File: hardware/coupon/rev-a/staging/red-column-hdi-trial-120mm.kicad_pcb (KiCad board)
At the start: 6 copper layers, 120 x 32.5 mm, 497 parts, among them J1 USB4505-03-0-A, J2 S2B-PH-SM4-TB, Q1 DMP2066LSN-7, Q10 DMP2066LSN-7, Q11 DMP2066LSN-7, Q12 DMP2066LSN-7, Q13 DMP2066LSN-7, Q14 DMP2066LSN-7, Q15 DMP2066LSN-7, Q16 DMP2066LSN-7, Q17 2N7002K-7, Q18 2N7002K-7, Q19 2N7002K-7, Q2 DMP2066LSN-7, Q20 2N7002K-7, Q21 2N7002K-7, Q22 2N7002K-7, Q23 2N7002K-7, Q24 2N7002K-7, Q25 2N7002K-7, Q26 2N7002K-7, Q27 2N7002K-7, Q28 2N7002K-7, Q29 2N7002K-7, Q3 DMP2066LSN-7, Q30 2N7002K-7, Q31 2N7002K-7, Q32 2N7002K-7, Q4 DMP2066LSN-7, Q5 DMP2066LSN-7, Q6 DMP2066LSN-7, Q7 DMP2066LSN-7, Q8 DMP2066LSN-7, Q9 DMP2066LSN-7, SW1 EVQP7J01P, SW2 JS202011JCQN, U1 TLC59581RTQT, U11 SN74LVC1G04DBVR, U17 SN74LVC1G11DBVR, U2 74HC4514PW,118, U23 SN74LVC1G06DBVR, U24 SN74LVC2G17DBVR, U25 SN74LVC2G17DBVR, U29 TPS70933DBVR, U3 ESP32-S3-WROOM-1U-N16R8, U31 TUSB320LAIRWBR, U32 TS3USB31ERSER, U33 TPD4E05U06DQAR, U34 TPS3808G01DBVR, U35 MAX17048G+T10, U36 TPS631000DRLR, U37 TPS63020DSJT, U38 2.5V shunt, U39 TMP390A2DRLR, U40 SN74AUP1G125DBVR, U41 BQ24074RGTR, U42 SN74AUP1G125DBVR, U43 SN74AUP1G125DBVR, U44 TPS259474ARPWR, U45 TPS259474ARPWR, U46 TCA9517ADGKR, U47 TPS3823A-33DBVR, U48 SN74LVC1G04DSFR, U49 SN74LVC1G74RSER, U50 SN74LVC1G74RSER, U51 SN74LVC1G11DRYR, U52 SN74LVC1G08DSFR, U53 TLV6700DSER, U54 SN74LVC2G00DCUR, U55 SN74LVC2G08DCUR

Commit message: Connect USB eFuse timing capacitor grounds in staged board
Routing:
- net GND: track 38.5 -> 53.3 mm, vias 9 -> 11

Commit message: Join second USB ground and charger-gate ground pad
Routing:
- net GND: track 53.3 -> 60.6 mm, vias 11 -> 12

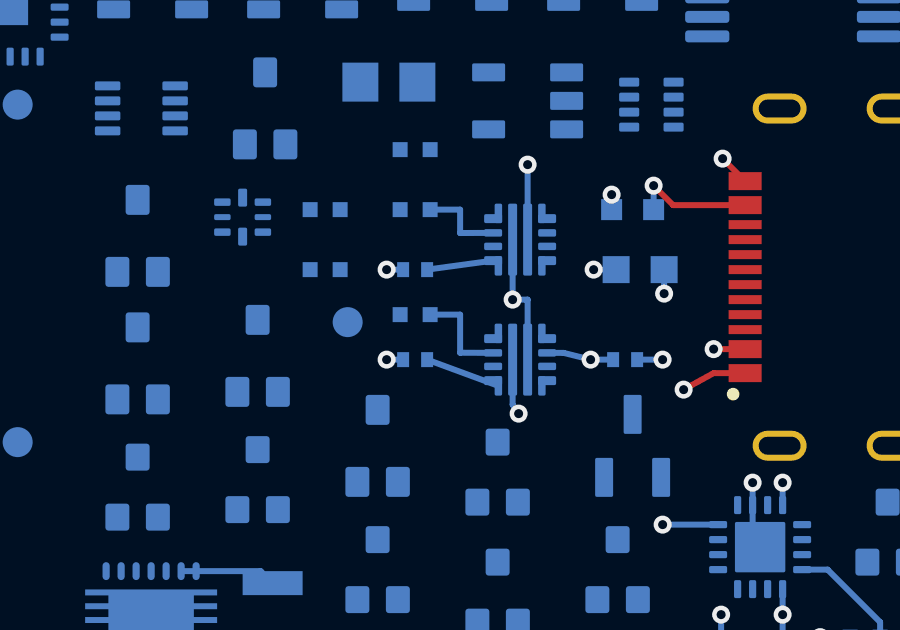
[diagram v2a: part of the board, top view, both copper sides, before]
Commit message: Connect both USB eFuse IC ground pins in staged board
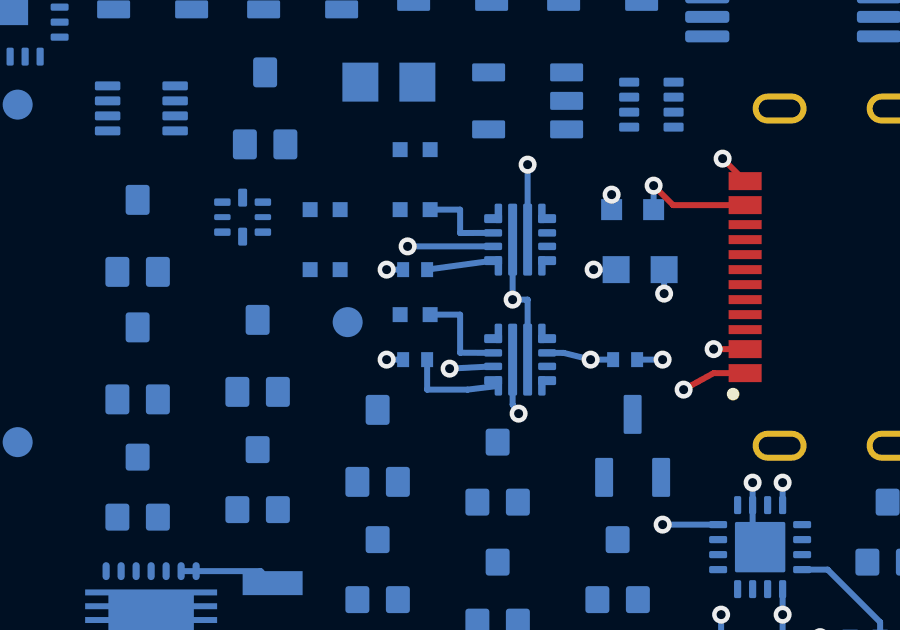
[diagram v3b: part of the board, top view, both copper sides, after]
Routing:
- net GND: track 60.6 -> 68.0 mm, vias 12 -> 14
- net E1_DVDT: track 2.53 -> 3.38 mm
